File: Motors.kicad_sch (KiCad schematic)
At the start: 6 parts, among them U8 DRV8876PWPR

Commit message: actualitzar ultrima versio pcb/esquematic
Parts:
- added C21: 10 u, Capacitor_SMD:C_0201_0603Metric, symbol Device:C
- added C22, C23: 100 n, Capacitor_SMD:C_0201_0603Metric, symbol Device:C
- added C24: 22 n, Capacitor_SMD:C_0201_0603Metric, symbol Device:C
- added J2, J8: Conn_01x02_Socket, Connector_JST:JST_PH_B2B-PH-K_1x02_P2.00mm_Vertical, symbol Connector:Conn_01x02_Socket
- added R21, R22, R23, R24, R25, R26, R27: R, Resistor_SMD:R_0201_0603Metric, symbol Device:R
- added U9: DRV8876PWPR, BQ25628E:WQFN-HR18__RYK_TEX, symbol DRV8876:DRV8876PWPR
- C10, C11, C12, C13: footprint (none) -> Capacitor_SMD:C_0201_0603Metric
- R14: value 1 k -> R; footprint (none) -> Resistor_SMD:R_0201_0603Metric
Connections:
- net +12V: now also R14.1, C21.1, C22.1, C23.2, R21.1, R23.1, R26.1, U9.11 (VM)
- net GND: now also U8.16 (PMODE), U8.7 (IMODE), U8.9 (PGND), C21.2, C22.2, R22.2, R24.2, R25.2, R27.2, U9.15 (GND), U9.16 (PMODE), U9.17 (PAD), U9.7 (IMODE), U9.9 (PGND)
- net at R14.2: now also R25.1, U9.5 (VREF)
- net EN/IN1: now reaches U8.1 (EN_IN1)
- net at U8.10 (OUT2): now also J2.2 (Pin_2)
- net PH/IN2: now reaches U8.2 (PH_IN2)
- net nSLEEP1: now reaches U8.3 (SLEEP_N)
- net nFAULT1: now reaches U8.4 (FAULT_N)
- net nFAULT1: now also R21.2
- net at U8.5 (VREF): now also R23.2, R24.1
- net IPROPI1: now reaches U8.6 (IPROPI)
- net IPROPI1: now also R22.1
- net at U8.8 (OUT1): now also J2.1 (Pin_1)
- new net: C23.1, U9.12 (VCP)
- new net: C24.1, U9.13 (CPH)
- new net: C24.2, U9.14 (CPL)
- new net: J8.1 (Pin_1), U9.8 (OUT1)
- new net: J8.2 (Pin_2), U9.10 (OUT2)
- new net EN/IN3: U9.1 (EN_IN1)
- new net IPROPI2: R27.1, U9.6 (IPROPI)
- new net PH/IN4: U9.2 (PH_IN2)
- new net nFAULT2: R26.2, U9.4 (FAULT_N)
- new net nSLEEP2: U9.3 (SLEEP_N)
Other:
- note removed: "Trip 1 A (1V)"
- moved on the sheet: C10, C11, C12, C13, U8

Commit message: arreclat footprints/symbol
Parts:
- U8: footprint PWP0016J_N -> dvr8876pwpr:PWP0016J_N
- U9: footprint BQ25628E:WQFN-HR18__RYK_TEX -> dvr8876pwpr:PWP0016J_N
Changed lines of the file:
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@@
 			)
 		)
-		(property "Footprint" "PWP0016J_N"
+		(property "Footprint" "dvr8876pwpr:PWP0016J_N"
 			(at 92.71 57.15 0)
 			(effects
@@
 			)
 		)
-		(property "Footprint" "BQ25628E:WQFN-HR18__RYK_TEX"
+		(property "Footprint" "dvr8876pwpr:PWP0016J_N"
 			(at 95.25 144.78 0)
 			(effects

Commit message: esquematic fet v1
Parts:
- C10, C11, C12, C13, C21, C22, C23, C24: footprint Capacitor_SMD:C_0201_0603Metric -> Capacitor_SMD:C_0603_1608Metric_Pad1.08x0.95mm_HandSolder
- R14, R21, R22, R23, R24, R25, R26, R27: footprint Resistor_SMD:R_0201_0603Metric -> Resistor_SMD:R_0603_1608Metric
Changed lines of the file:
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@@
 			)
 		)
-		(property "Footprint" "Capacitor_SMD:C_0201_0603Metric"
+		(property "Footprint" "Capacitor_SMD:C_0603_1608Metric_Pad1.08x0.95mm_HandSolder"
 			(at 63.8048 116.84 0)
 			(effects
@@
 			)
 		)
-		(property "Footprint" "Capacitor_SMD:C_0201_0603Metric"
+		(property "Footprint" "Capacitor_SMD:C_0603_1608Metric_Pad1.08x0.95mm_HandSolder"
 			(at 122.8852 154.94 0)
 			(effects
@@
 			)
 		)
-		(property "Footprint" "Capacitor_SMD:C_0201_0603Metric"
+		(property "Footprint" "Capacitor_SMD:C_0603_1608Metric_Pad1.08x0.95mm_HandSolder"
 			(at 40.3352 124.46 0)
 			(effects
@@
 			)
 		)
-		(property "Footprint" "Resistor_SMD:R_0201_0603Metric"
+		(property "Footprint" "Resistor_SMD:R_0603_1608Metric"
 			(at 21.082 148.59 90)
 			(effects
@@
 			)
 		)
-		(property "Footprint" "Resistor_SMD:R_0201_0603Metric"
+		(property "Footprint" "Resistor_SMD:R_0603_1608Metric"
 			(at 18.542 73.66 90)
 			(effects
@@
 			)
 		)
-		(property "Footprint" "Resistor_SMD:R_0201_0603Metric"
+		(property "Footprint" "Resistor_SMD:R_0603_1608Metric"
 			(at 43.942 78.74 90)
 			(effects
@@
 			)
 		)
-		(property "Footprint" "Resistor_SMD:R_0201_0603Metric"
+		(property "Footprint" "Resistor_SMD:R_0603_1608Metric"
 			(at 43.942 55.88 90)
 			(effects
@@
 			)
 		)
-		(property "Footprint" "Capacitor_SMD:C_0201_0603Metric"
+		(property "Footprint" "Capacitor_SMD:C_0603_1608Metric_Pad1.08x0.95mm_HandSolder"
 			(at 37.7952 36.83 0)
 			(effects
@@
 			)
 		)
-		(property "Footprint" "Resistor_SMD:R_0201_0603Metric"
+		(property "Footprint" "Resistor_SMD:R_0603_1608Metric"
 			(at 46.482 143.51 90)
 			(effects
@@
 			)
 		)
-		(property "Footprint" "Capacitor_SMD:C_0201_0603Metric"
+		(property "Footprint" "Capacitor_SMD:C_0603_1608Metric_Pad1.08x0.95mm_HandSolder"
 			(at 51.7652 124.46 0)
 			(effects
@@
 			)
 		)
-		(property "Footprint" "Capacitor_SMD:C_0201_0603Metric"
+		(property "Footprint" "Capacitor_SMD:C_0603_1608Metric_Pad1.08x0.95mm_HandSolder"
 			(at 120.3452 67.31 0)
 			(effects
@@
 			)
 		)
-		(property "Footprint" "Resistor_SMD:R_0201_0603Metric"
+		(property "Footprint" "Resistor_SMD:R_0603_1608Metric"
 			(at 18.542 60.96 90)
 			(effects
@@
 			)
 		)
-		(property "Footprint" "Resistor_SMD:R_0201_0603Metric"
+		(property "Footprint" "Resistor_SMD:R_0603_1608Metric"
 			(at 21.082 161.29 90)
 			(effects
@@
 			)
 		)
-		(property "Footprint" "Resistor_SMD:R_0201_0603Metric"
+		(property "Footprint" "Resistor_SMD:R_0603_1608Metric"
 			(at 46.482 166.37 90)
 			(effects
@@
 			)
 		)
-		(property "Footprint" "Capacitor_SMD:C_0201_0603Metric"
+		(property "Footprint" "Capacitor_SMD:C_0603_1608Metric_Pad1.08x0.95mm_HandSolder"
 			(at 49.2252 36.83 0)
 			(effects
@@
 			)
 		)
-		(property "Footprint" "Capacitor_SMD:C_0201_0603Metric"
+		(property "Footprint" "Capacitor_SMD:C_0603_1608Metric_Pad1.08x0.95mm_HandSolder"
 			(at 61.2648 29.21 0)
 			(effects

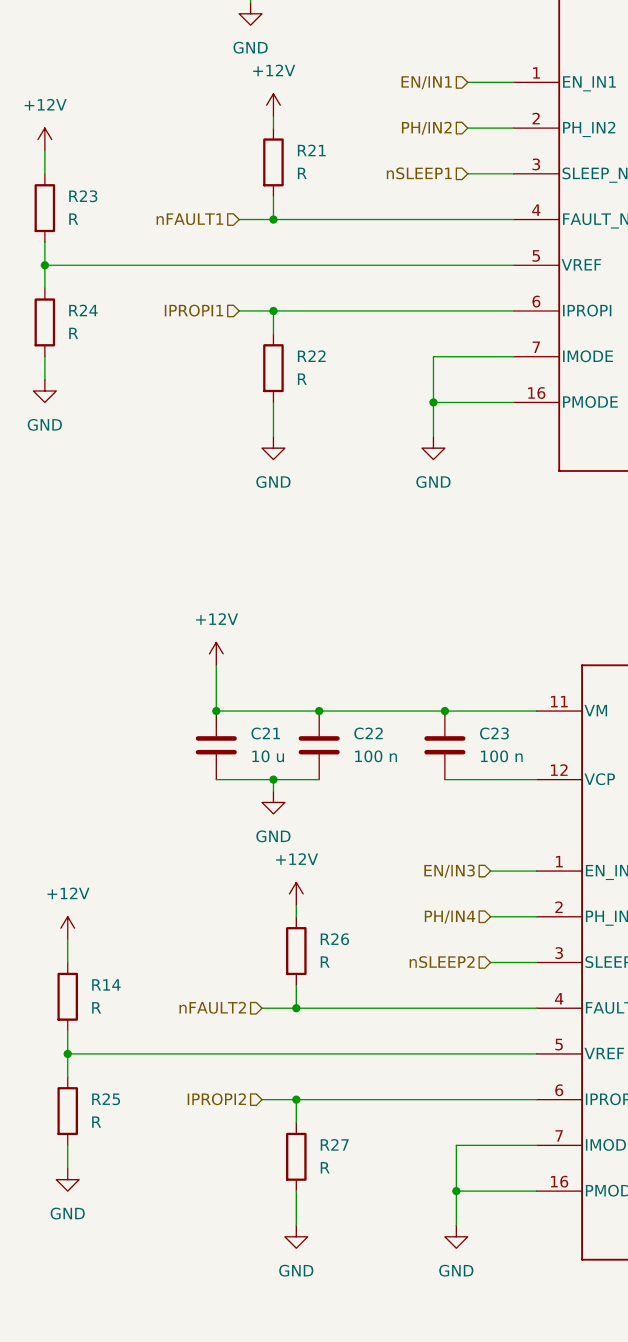
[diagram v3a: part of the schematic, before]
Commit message: Actualitzats valors dels components
S'han actualitzat els valors de components d'acord als comprats, s'ha canviat algun valor per conveniència, i s'ha acabat de donar valors a tots els components
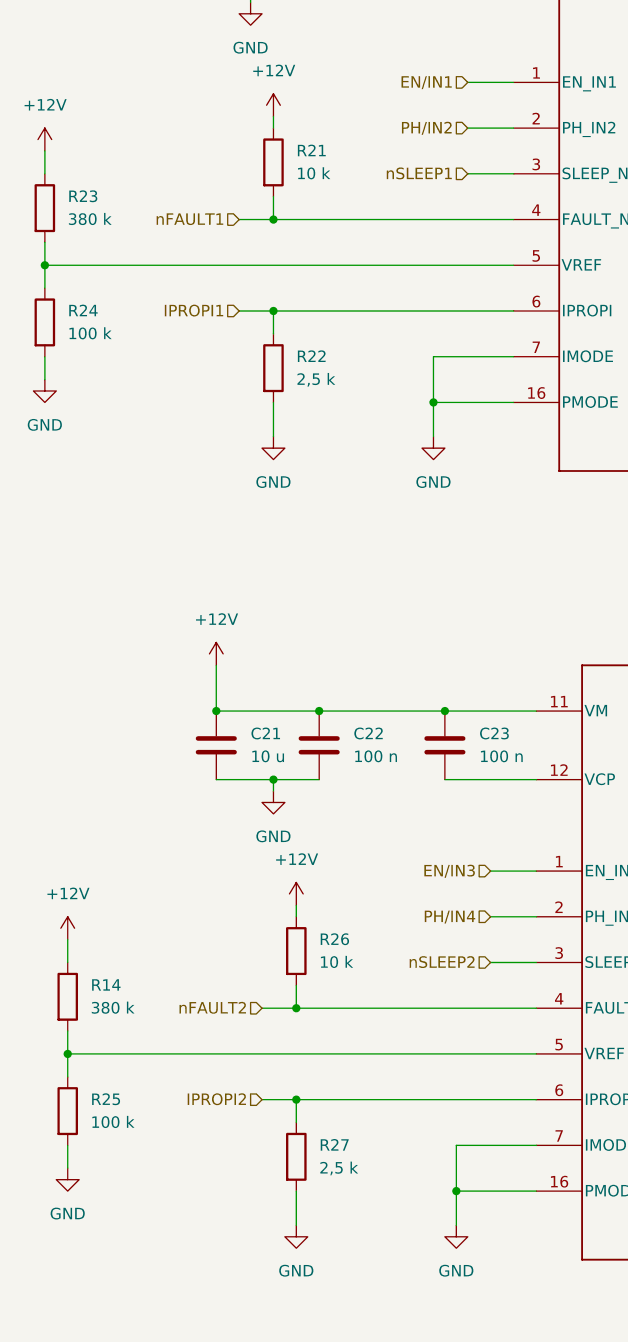
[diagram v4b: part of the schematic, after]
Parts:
- R14, R23: value R -> 380 k
- R21, R26: value R -> 10 k
- R22, R27: value R -> 2,5 k
- R24, R25: value R -> 100 k
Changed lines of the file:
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@@
 		(shape input)
 		(at 44.45 149.86 180)
-		(fields_autoplaced yes)
 		(effects
 			(font
@@
 		(shape input)
 		(at 41.91 72.39 180)
-		(fields_autoplaced yes)
 		(effects
 			(font
@@
 		(shape input)
 		(at 69.85 139.7 180)
-		(fields_autoplaced yes)
 		(effects
 			(font
@@
 		(shape input)
 		(at 44.45 160.02 180)
-		(fields_autoplaced yes)
 		(effects
 			(font
@@
 		(shape input)
 		(at 67.31 52.07 180)
-		(fields_autoplaced yes)
 		(effects
 			(font
@@
 		(shape input)
 		(at 41.91 62.23 180)
-		(fields_autoplaced yes)
 		(effects
 			(font
@@
 		(shape input)
 		(at 67.31 46.99 180)
-		(fields_autoplaced yes)
 		(effects
 			(font
@@
 		(shape input)
 		(at 67.31 57.15 180)
-		(fields_autoplaced yes)
 		(effects
 			(font
@@
 		(shape input)
 		(at 69.85 134.62 180)
-		(fields_autoplaced yes)
 		(effects
 			(font
@@
 		(shape input)
 		(at 69.85 144.78 180)
-		(fields_autoplaced yes)
 		(effects
 			(font
@@
 			)
 		)
-		(property "Value" "R"
+		(property "Value" "380 k"
 			(at 25.4 149.8599 0)
 			(effects
@@
 			)
 		)
-		(property "Value" "R"
+		(property "Value" "100 k"
 			(at 22.86 74.9299 0)
 			(effects
@@
 			)
 		)
-		(property "Value" "R"
+		(property "Value" "2,5 k"
 			(at 48.26 80.0099 0)
 			(effects
@@
 			)
 		)
-		(property "Value" "R"
+		(property "Value" "10 k"
 			(at 48.26 57.1499 0)
 			(effects
@@
 			)
 		)
-		(property "Value" "R"
+		(property "Value" "10 k"
 			(at 50.8 144.7799 0)
 			(effects
@@
 			)
 		)
-		(property "Value" "R"
+		(property "Value" "380 k"
 			(at 22.86 62.2299 0)
 			(effects
@@
 			)
 		)
-		(property "Value" "R"
+		(property "Value" "100 k"
 			(at 25.4 162.5599 0)
 			(effects
@@
 			)
 		)
-		(property "Value" "R"
+		(property "Value" "2,5 k"
 			(at 50.8 167.6399 0)
 			(effects
